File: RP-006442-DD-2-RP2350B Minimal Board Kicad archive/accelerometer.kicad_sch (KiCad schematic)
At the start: 4 parts, among them U12 LIS2DW12TR

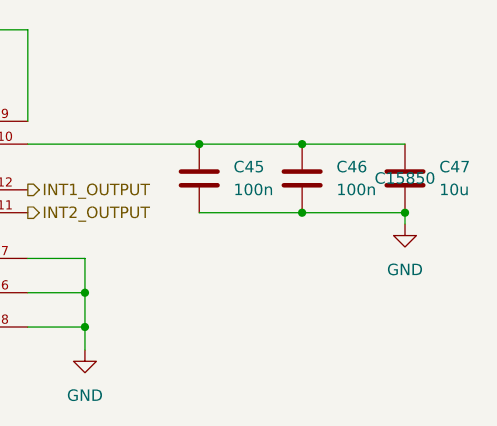
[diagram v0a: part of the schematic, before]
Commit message: New Flash memory footprint
footprint from snapmagic
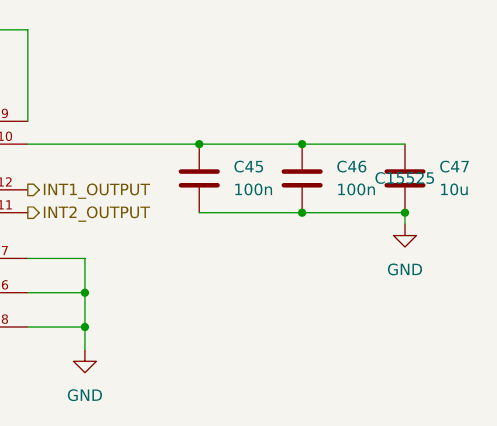
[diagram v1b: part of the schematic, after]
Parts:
- C47: LCSC C15850 -> C15525
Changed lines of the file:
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@@
 			)
 		)
-		(property "LCSC" "C15850"
+		(property "LCSC" "C15525"
 			(at 207.01 97.79 0)
 			(effects

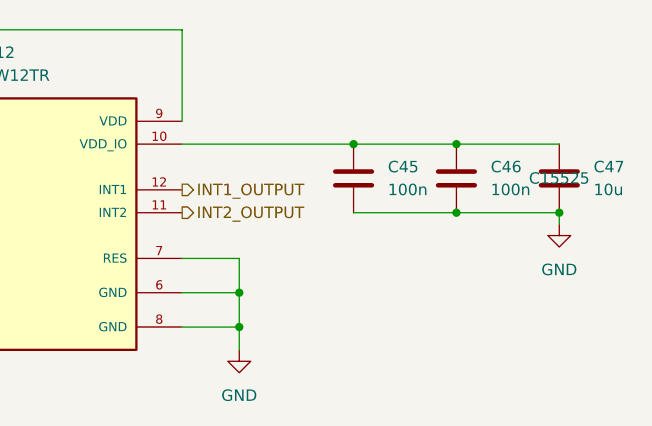
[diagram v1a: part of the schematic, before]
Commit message: Added MMA8451QR1 symbol and footprint
MMA8451QR1 Accelerometer
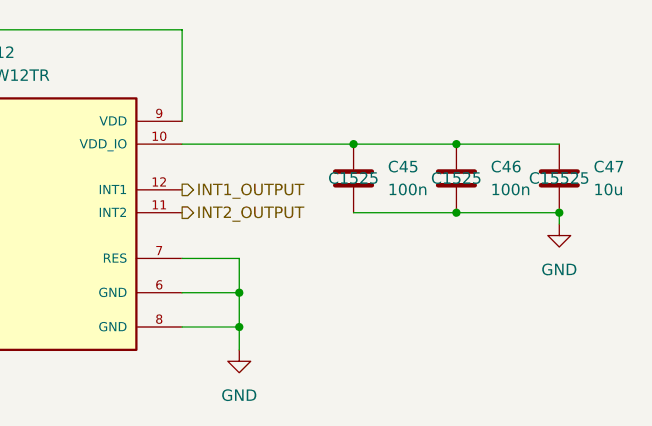
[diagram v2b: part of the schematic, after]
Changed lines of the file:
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@@
-					(size 1.27 1.27)
-				)
-				(hide yes)
-			)
-		)
-		(property "LSCS" ""
-			(at 184.15 97.79 0)
-			(effects
-				(font
 					(size 1.27 1.27)
 				)
@@
 			(at 195.58 97.79 0)
 			(effects
-				(font
-					(size 1.27 1.27)
-				)
-				(hide yes)
-			)
-		)
-		(property "LSCS" ""
-			(at 195.58 97.79 0)
-			(effects

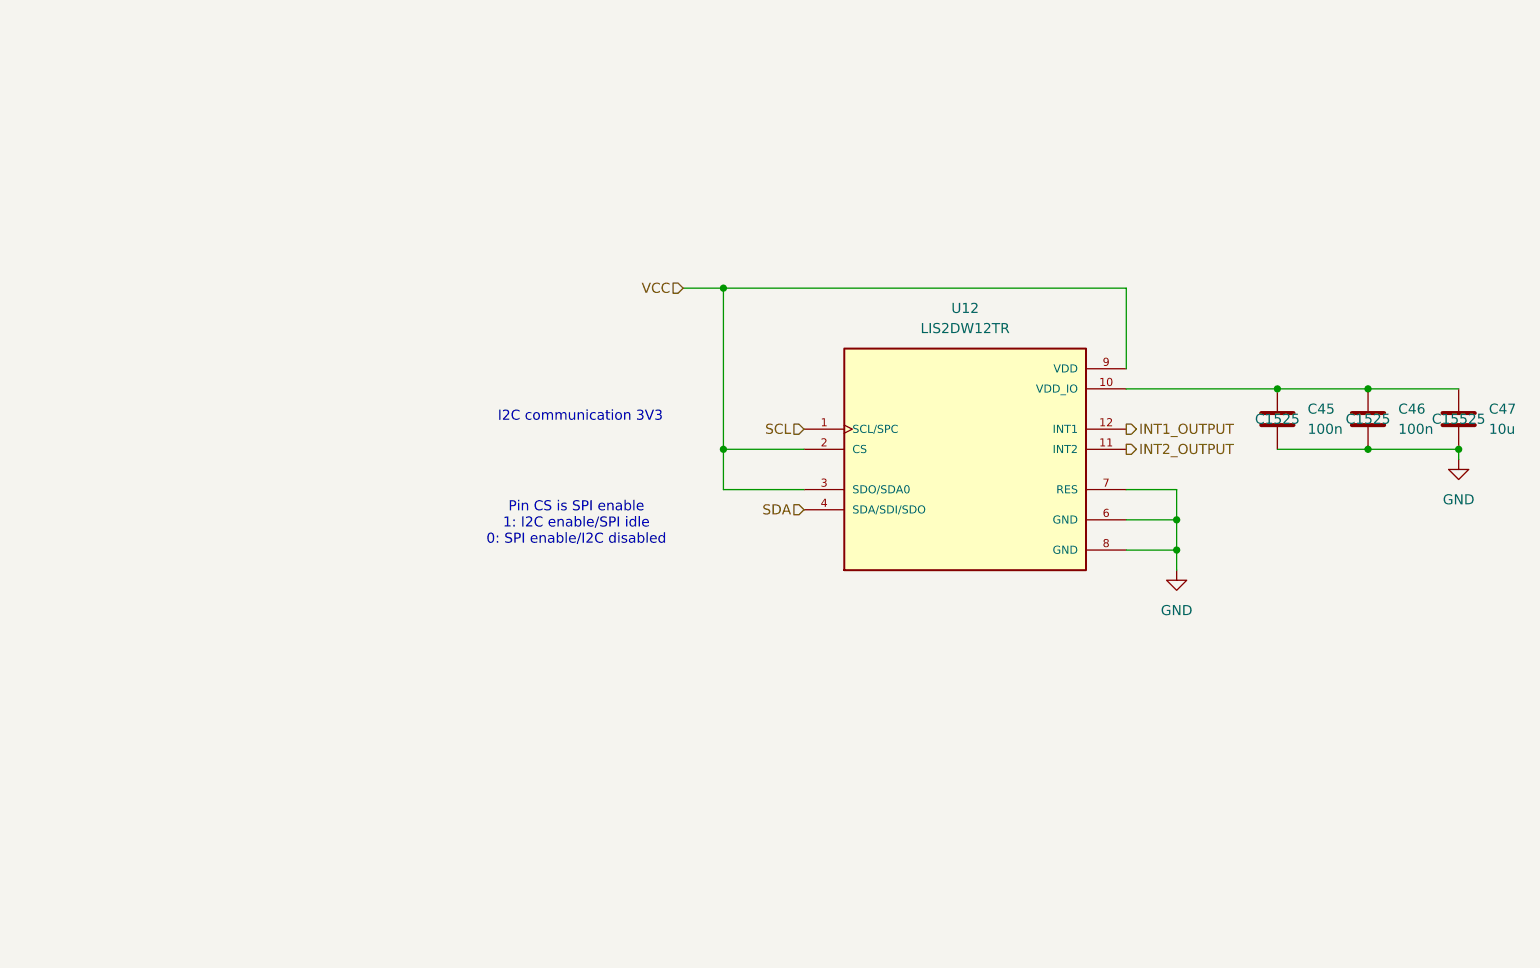
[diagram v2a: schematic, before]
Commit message: New accelerometer schematic
MMA8451QR1
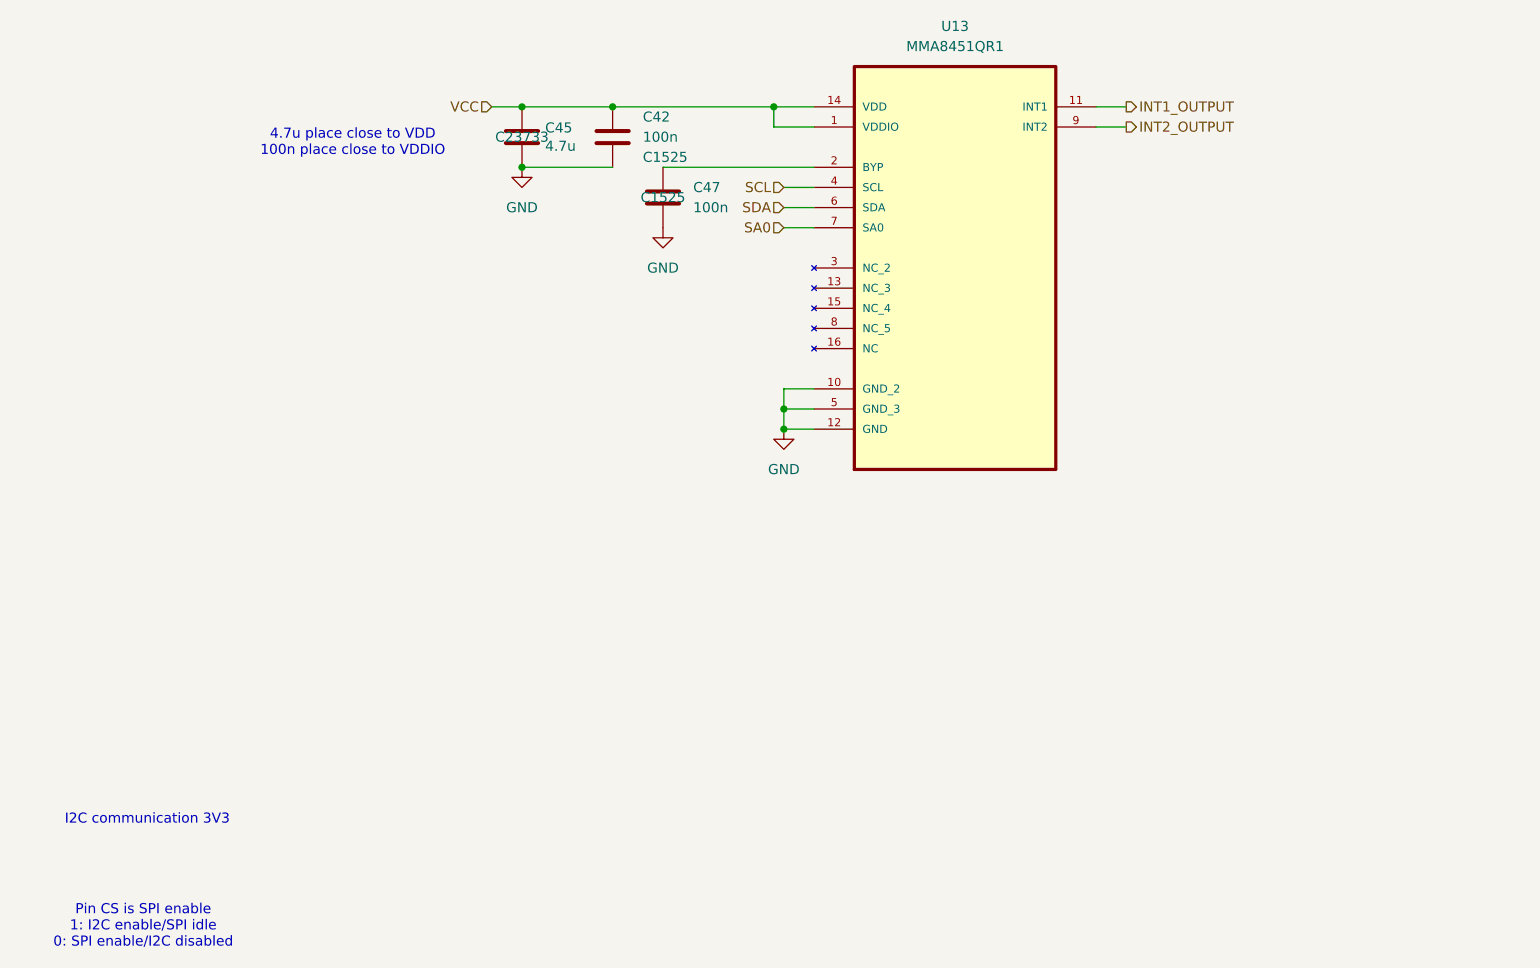
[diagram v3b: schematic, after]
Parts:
- removed U12: LIS2DW12TR, LIS2DW12TR:LGA12R50P4X4_200X200X70, symbol LIS2DW12TR:LIS2DW12TR
- added U13: MMA8451QR1, MMA8451QR1:QFN50P300X300X100-16N, symbol MMA8451QR1:MMA8451QR1
- C45: value 100n -> 4.7u; LCSC C1525 -> C23733
- C47: value 10u -> 100n; LCSC C15525 -> C1525
- renumbered C46 to C42
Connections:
- net GND: now also U13.10 (GND_2), U13.12 (GND), U13.5 (GND_3)
- net INT1_OUTPUT: now also U13.11 (INT1)
- net INT2_OUTPUT: now also U13.9 (INT2)
- net SCL: now also U13.4 (SCL)
- net SDA: now also U13.6 (SDA)
- net VCC: now also C42.1, C45.1, U13.1 (VDDIO), U13.14 (VDD)
- new net: C47.1, U13.2 (BYP)
- new net SA0: U13.7 (SA0)
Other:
- note added: "4.7u place close to VDD 100n place close to VDDIO"
- moved on the sheet: C42
